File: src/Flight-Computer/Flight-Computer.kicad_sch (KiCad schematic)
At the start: 40 parts, among them J1 Jumper_NO, P1 282837-2, P2 647676-2, P8 3220-20-0200-00, U1 STM32H750VBTx, U2 LMS8117AMP-3.3_NOPB, Y1 ECS-240-18-33-JGN-TR

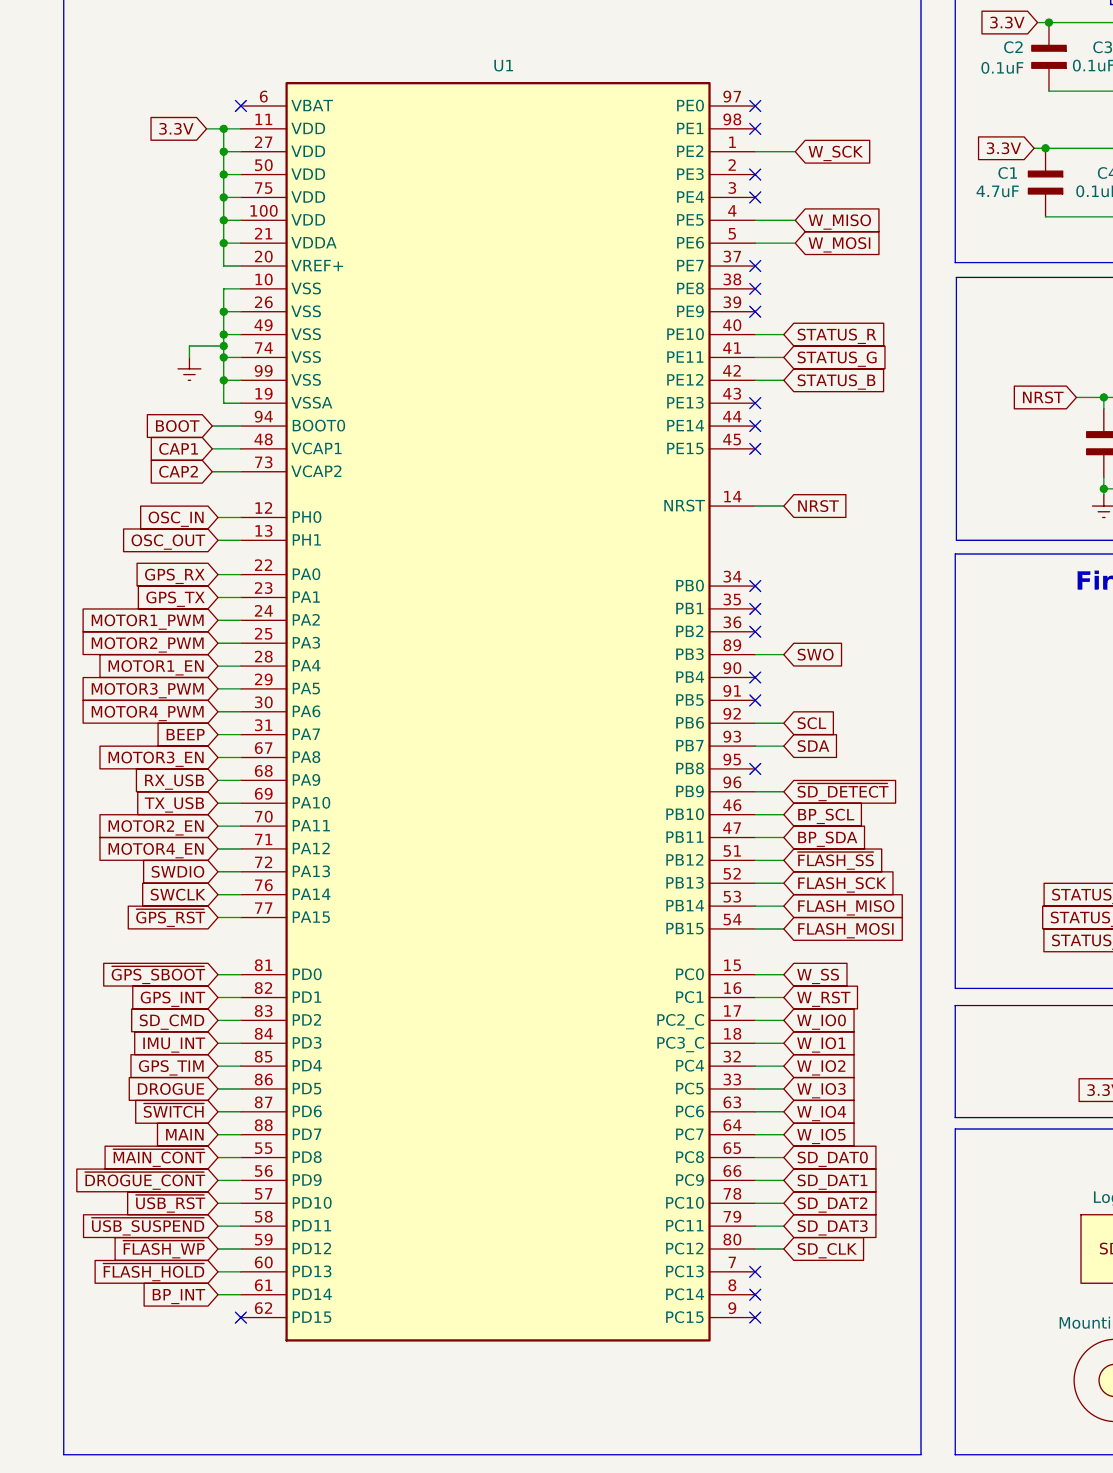
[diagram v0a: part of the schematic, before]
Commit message: routed main peripheral functionality excluding parachute deployment circuitry
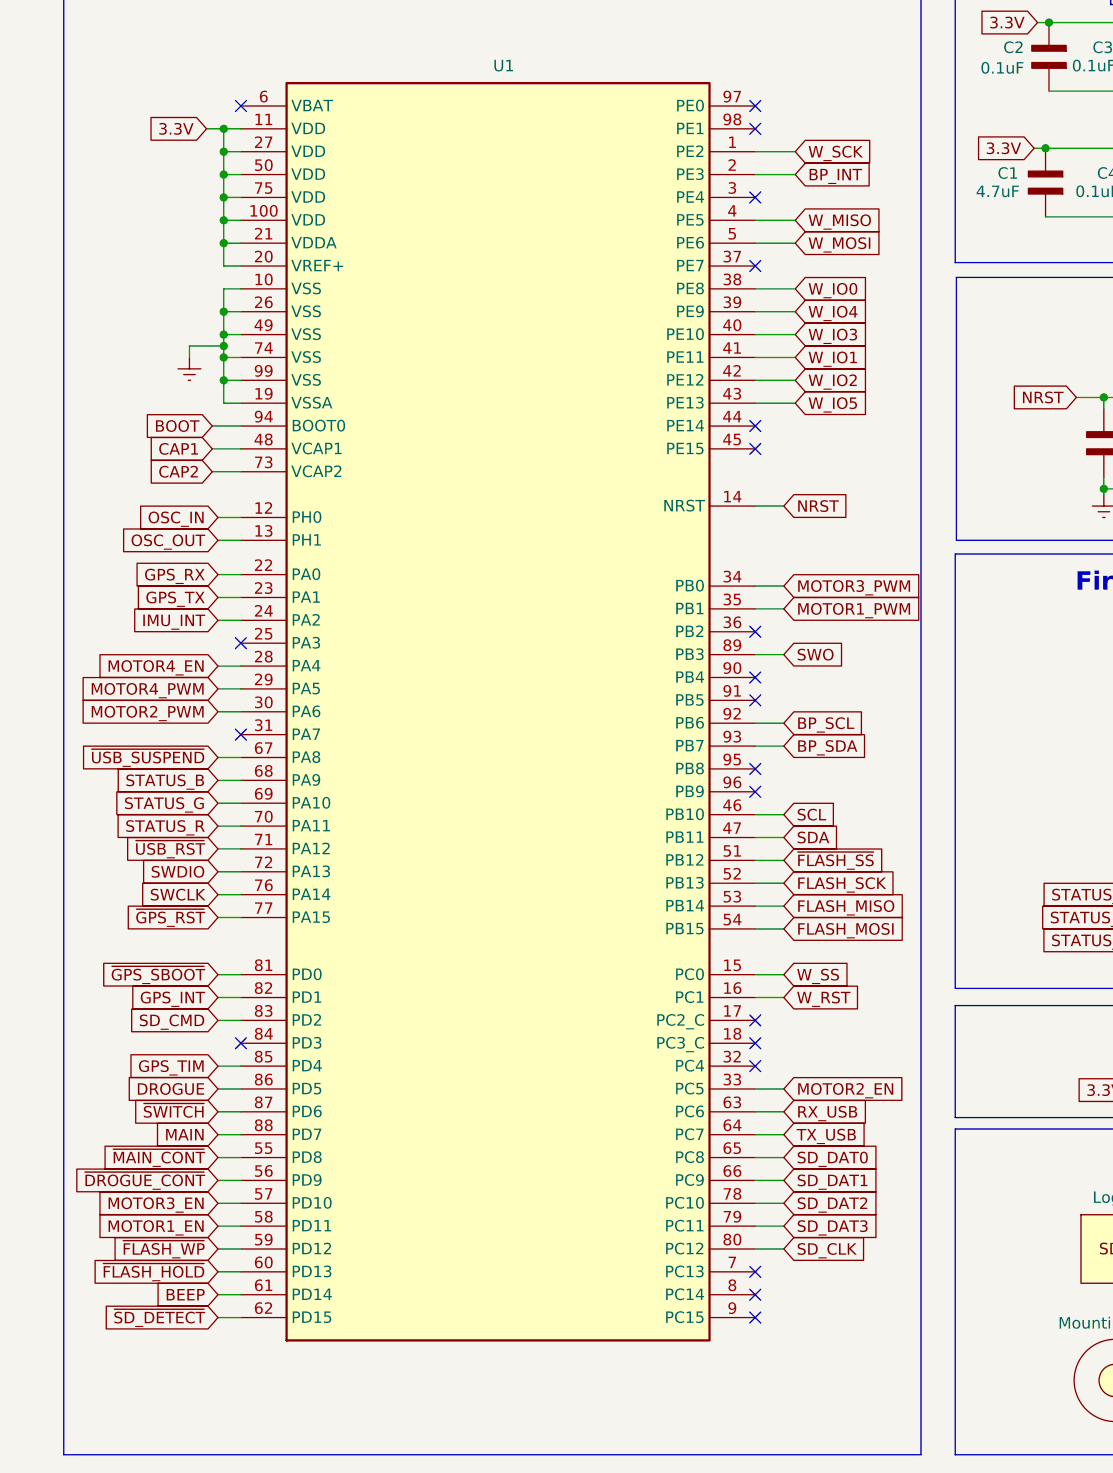
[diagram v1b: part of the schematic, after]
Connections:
- net BEEP: now also U1.61 (PD14); no longer U1.31 (PA7)
- net BP_INT: now also U1.2 (PE3); no longer U1.61 (PD14)
- net BP_SCL: now also U1.92 (PB6); no longer U1.46 (PB10)
- net BP_SDA: now also U1.93 (PB7); no longer U1.47 (PB11)
- net IMU_INT: now also U1.24 (PA2); no longer U1.84 (PD3)
- net MOTOR1_EN: now also U1.58 (PD11); no longer U1.28 (PA4)
- net MOTOR1_PWM: now also U1.35 (PB1); no longer U1.24 (PA2)
- net MOTOR2_EN: now also U1.33 (PC5); no longer U1.70 (PA11)
- net MOTOR2_PWM: now also U1.30 (PA6); no longer U1.25 (PA3)
- net MOTOR3_EN: now also U1.57 (PD10); no longer U1.67 (PA8)
- net MOTOR3_PWM: now also U1.34 (PB0); no longer U1.29 (PA5)
- net MOTOR4_EN: now also U1.28 (PA4); no longer U1.71 (PA12)
- net MOTOR4_PWM: now also U1.29 (PA5); no longer U1.30 (PA6)
- net RX_USB: now also U1.63 (PC6); no longer U1.68 (PA9)
- net SCL: now also U1.46 (PB10); no longer U1.92 (PB6)
- net SDA: now also U1.47 (PB11); no longer U1.93 (PB7)
- net STATUS_B: now also U1.68 (PA9); no longer U1.42 (PE12)
- net STATUS_G: now also U1.69 (PA10); no longer U1.41 (PE11)
- net STATUS_R: now also U1.70 (PA11); no longer U1.40 (PE10)
- net TX_USB: now also U1.64 (PC7); no longer U1.69 (PA10)
- net W_IO0: now also U1.38 (PE8); no longer U1.17 (PC2_C)
- net W_IO1: now also U1.41 (PE11); no longer U1.18 (PC3_C)
- net W_IO2: now also U1.42 (PE12); no longer U1.32 (PC4)
- net W_IO3: now also U1.40 (PE10); no longer U1.33 (PC5)
- net W_IO4: now also U1.39 (PE9); no longer U1.63 (PC6)
- net W_IO5: now also U1.43 (PE13); no longer U1.64 (PC7)
- net ~{SD_DETECT}: now also U1.62 (PD15); no longer U1.96 (PB9)
- net ~{USB_RST}: now also U1.71 (PA12); no longer U1.57 (PD10)
- net ~{USB_SUSPEND}: now also U1.67 (PA8); no longer U1.58 (PD11)

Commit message: finished routing
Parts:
- removed TP1: TP, Flight-Computer:TP, symbol Flight-Computer:TP
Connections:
- net DROGUE: now also U1.7 (PC13); no longer U1.86 (PD5)
- net GPS_INT: now also U1.25 (PA3); no longer U1.82 (PD1)
- net GPS_TIM: now also U1.32 (PC4); no longer U1.85 (PD4)
- net MAIN: now also U1.87 (PD6); no longer U1.88 (PD7)
- net W_IO1: now also U1.40 (PE10); no longer U1.41 (PE11)
- net W_IO3: now also U1.41 (PE11); no longer U1.40 (PE10)
- net ~{DROGUE_CONT}: now also U1.8 (PC14); no longer U1.56 (PD9)
- net ~{GPS_RST}: now also U1.31 (PA7); no longer U1.77 (PA15)
- net ~{GPS_SBOOT}: now also U1.9 (PC15); no longer U1.81 (PD0)
- net ~{MAIN_CONT}: now also U1.3 (PE4); no longer U1.55 (PD8)
- net ~{SWITCH}: now also U1.88 (PD7); no longer U1.87 (PD6)
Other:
- moved on the sheet: B1, C8

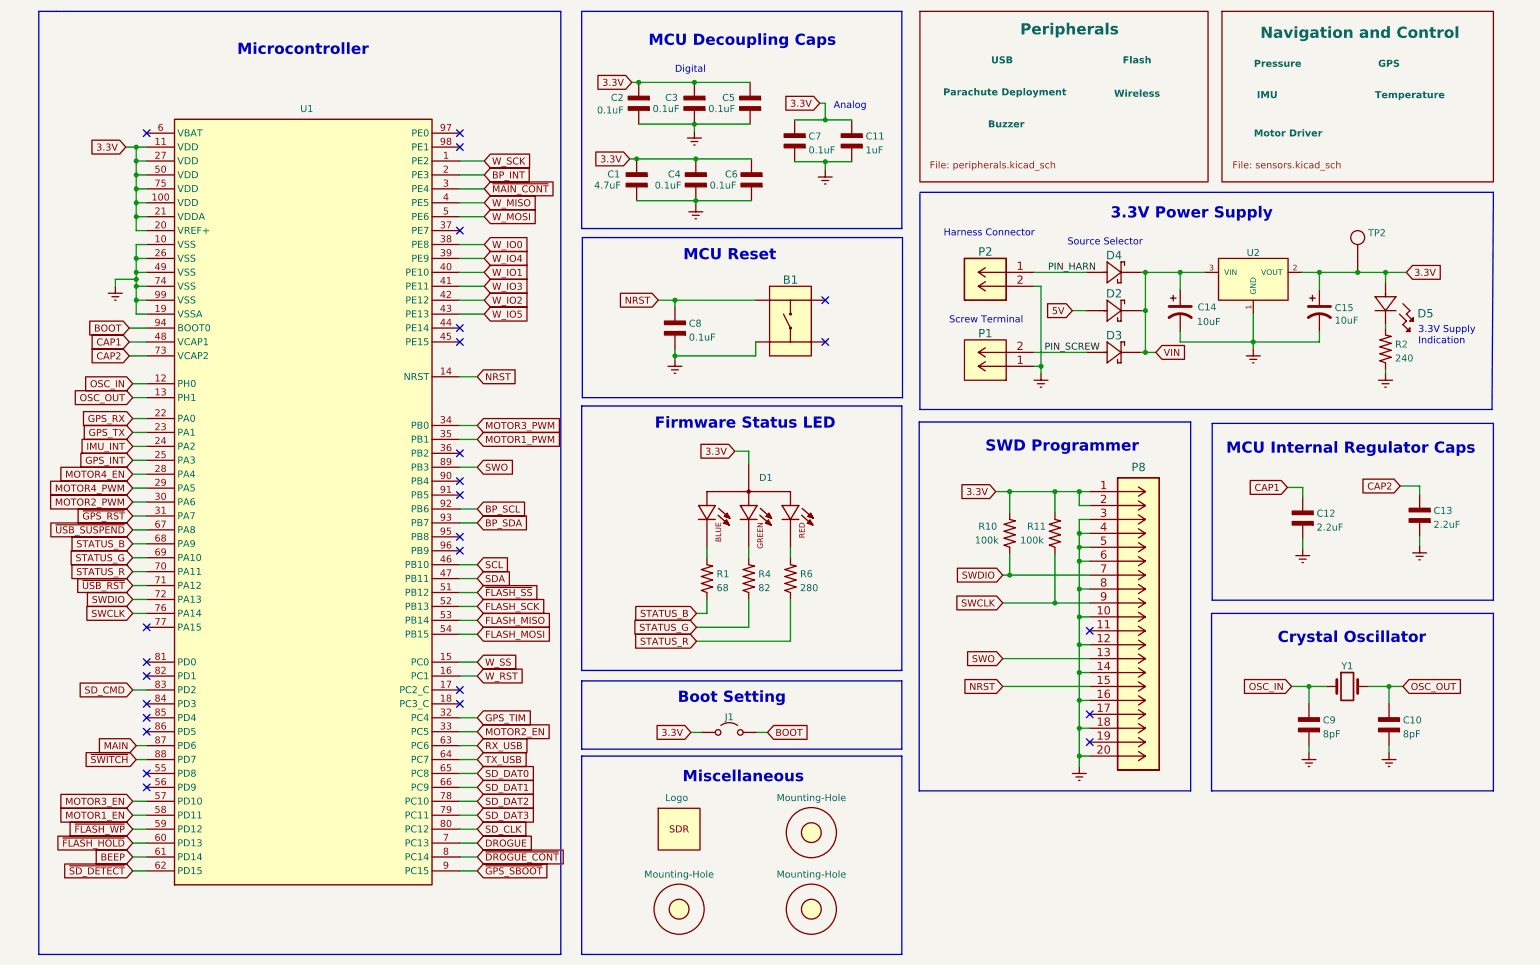
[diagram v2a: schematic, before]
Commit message: added usb detector to schemtaic
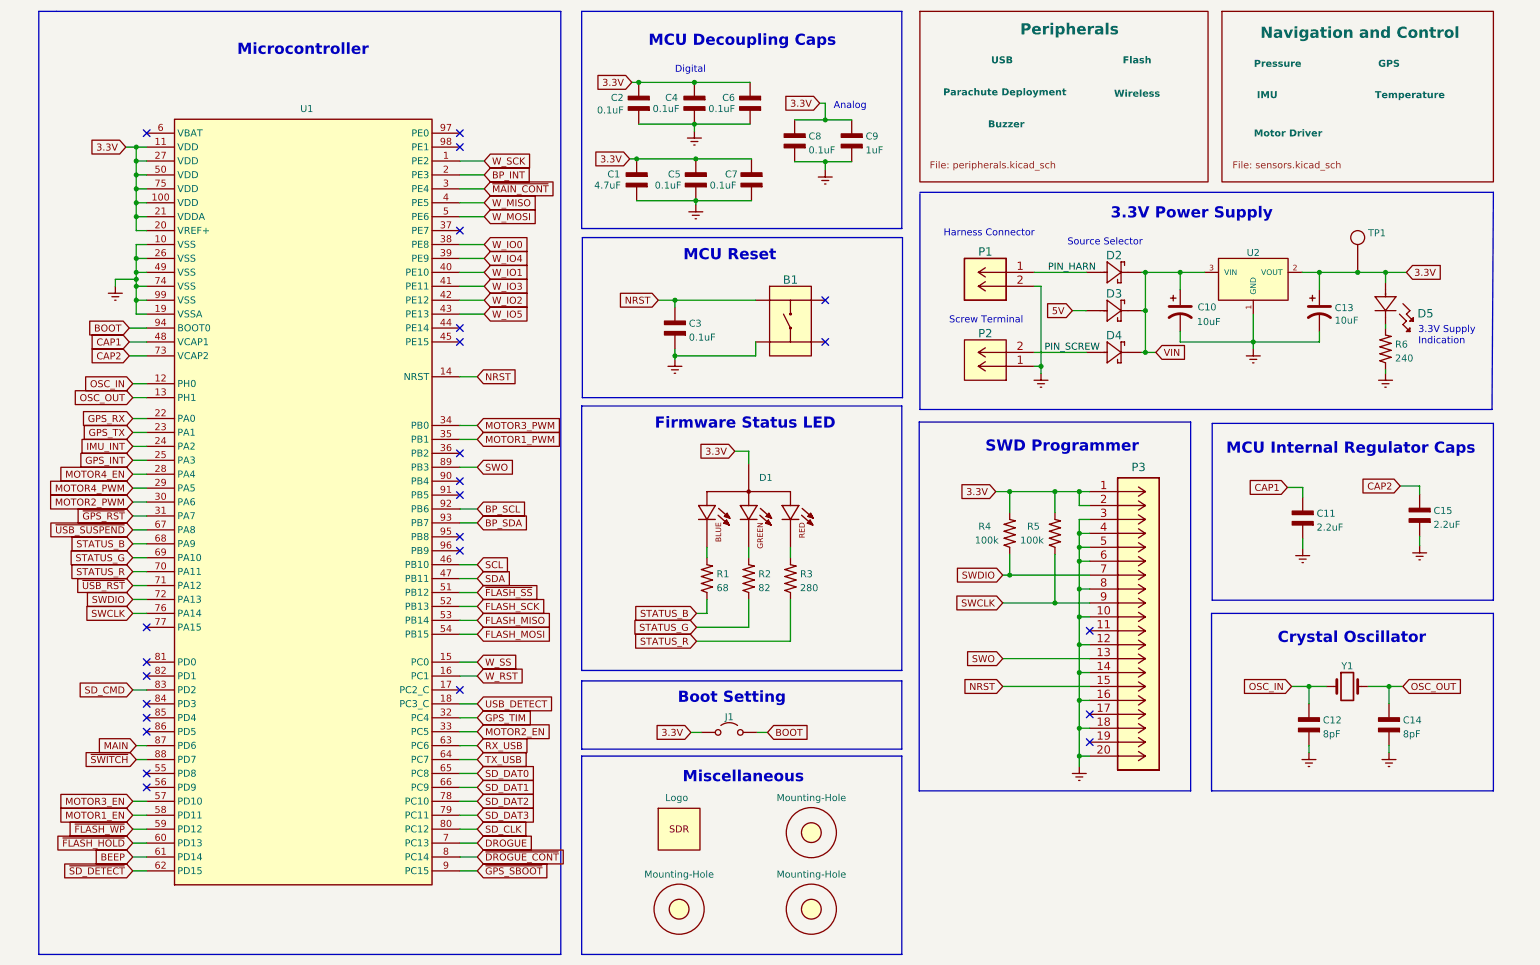
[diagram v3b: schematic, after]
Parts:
- renumbered C14 to C10, C12 to C11, C9 to C12, C15 to C13, C10 to C14, C13 to C15, C8 to C3, C3 to C4, C4 to C5, C5 to C6, C6 to C7, C7 to C8, C11 to C9, D4 to D2, D2 to D3, D3 to D4, H3 to H2, H4 to H3, P2 to P1, P1 to P2, P8 to P3, R4 to R2, R6 to R3, R10 to R4, R11 to R5, R2 to R6, TP2 to TP1
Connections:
- net USB_DETECT: now reaches U1.18 (PC3_C)
- no-connect marks 26 -> 25

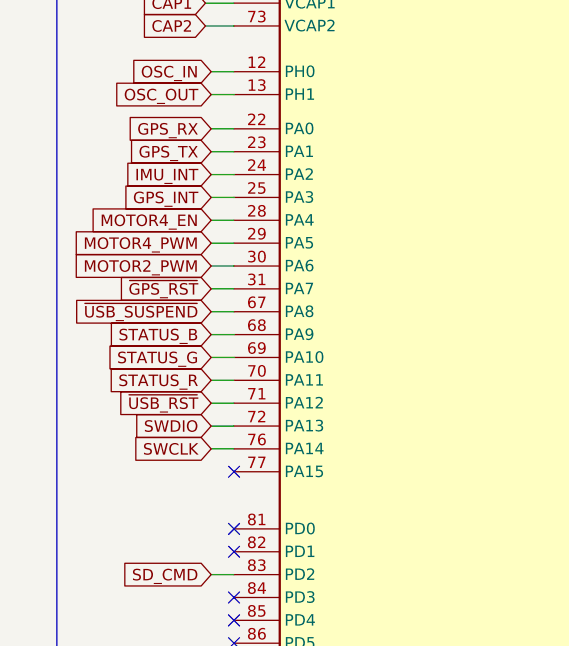
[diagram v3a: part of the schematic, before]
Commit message: implemented new imu in schematic
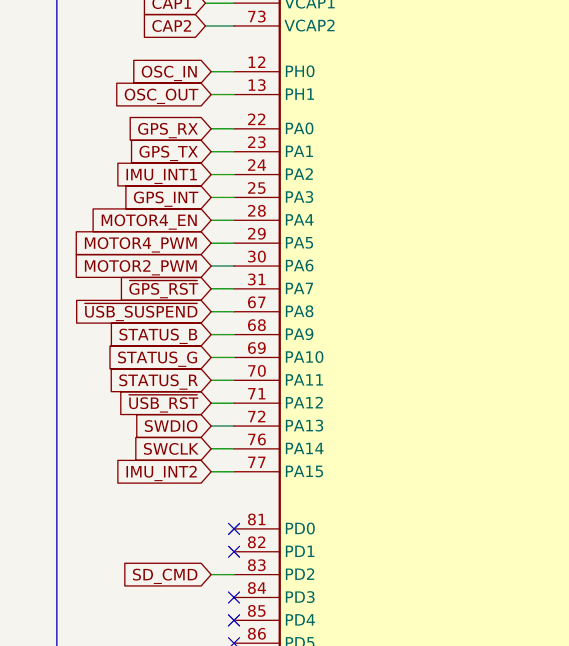
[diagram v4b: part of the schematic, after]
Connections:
- net IMU_INT2: now reaches U1.77 (PA15)
- net IMU_INT renamed IMU_INT1
- no-connect marks 25 -> 24
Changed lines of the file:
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@@
   (no_connect (at 36.195 160.655))
   (no_connect (at 93.345 79.375))
-  (no_connect (at 36.195 131.445))
   (no_connect (at 93.345 41.275))
   (no_connect (at 36.195 137.795))
@@
     (stroke (width 0) (type default) (color 0 0 0 0))
   )
+  (wire (pts (xy 33.655 131.445) (xy 36.195 131.445))
+    (stroke (width 0) (type default) (color 0 0 0 0))
+  )
   (wire (pts (xy 33.655 108.585) (xy 36.195 108.585))
     (stroke (width 0) (type default) (color 0 0 0 0))
@@
     )
   )
-  (global_label "IMU_INT" (shape input) (at 33.655 98.425 180) (fields_autoplaced)
-    (effects (font (size 1.27 1.27)) (justify right))
-    (property "Intersheet References" "${INTERSHEET_REFS}" (id 0) (at 24.0737 98.5044 0)
+  (global_label "IMU_INT1" (shape input) (at 33.655 98.425 180) (fields_autoplaced)
+    (effects (font (size 1.27 1.27)) (justify right))
+    (property "Intersheet References" "${INTERSHEET_REFS}" (id 0) (at 22.8641 98.3456 0)
       (effects (font (size 1.27 1.27)) (justify right) hide)
     )
@@
     (property "Intersheet References" "${INTERSHEET_REFS}" (id 0) (at 106.8271 163.1156 0)
       (effects (font (size 1.27 1.27)) (justify left) hide)
+    )
+  )
+  (global_label "IMU_INT2" (shape input) (at 33.655 131.445 180) (fields_autoplaced)
+    (effects (font (size 1.27 1.27)) (justify right))
+    (property "Intersheet References" "${INTERSHEET_REFS}" (id 0) (at 22.8641 131.3656 0)
+      (effects (font (size 1.27 1.27)) (justify right) hide)
     )
   )
@@
       (reference "#PWR016") (unit 1) (value "Earth") (footprint "")
     )
-    (path "/a7215684-cee9-4aba-87f1-e5962f77da19/1082dc28-77e5-4081-9653-ba3ccdcff140"
+    (path "/a7215684-cee9-4aba-87f1-e5962f77da19/9a733085-ccb6-4e9a-ae63-1f8c81139c23"
       (reference "#PWR017") (unit 1) (value "Earth") (footprint "")
     )
-    (path "/a7215684-cee9-4aba-87f1-e5962f77da19/3a528831-3703-47fa-b2f9-9d35d9a4482a"
+    (path "/a7215684-cee9-4aba-87f1-e5962f77da19/4f903274-7819-4ad4-9ef1-7cd0982c653d"
       (reference "#PWR018") (unit 1) (value "Earth") (footprint "")
     )
@@
       (reference "#PWR019") (unit 1) (value "Earth") (footprint "")
     )
-    (path "/a7215684-cee9-4aba-87f1-e5962f77da19/34f9584b-e14b-4f45-b1d8-6cf67f13081e"
-      (reference "#PWR020") (unit 1) (value "Earth") (footprint "")
-    )
-    (path "/a7215684-cee9-4aba-87f1-e5962f77da19/4bd954ef-7b24-4be2-9e47-dffb88431f61"
-      (reference "#PWR021") (unit 1) (value "Earth") (footprint "")
-    )
     (path "/a7215684-cee9-4aba-87f1-e5962f77da19/4b71cbdc-b374-4c43-a5ca-debee457df14"
       (reference "#PWR022") (unit 1) (value "Earth") (footprint "")
@@
       (reference "C16") (unit 1) (value "0.01uF") (footprint "Flight-Computer:CAP_0603")
     )
-    (path "/a7215684-cee9-4aba-87f1-e5962f77da19/ac484fe8-f18d-49d6-9d61-7cc144d8f31c"
+    (path "/a7215684-cee9-4aba-87f1-e5962f77da19/a0cd1c44-a6aa-4d8b-a2b3-df49039d37ee"
       (reference "C17") (unit 1) (value "0.1uF") (footprint "Flight-Computer:CAP_0603")
     )
-    (path "/a7215684-cee9-4aba-87f1-e5962f77da19/3008f6fe-df75-4af1-928e-60f268f36a31"
+    (path "/a7215684-cee9-4aba-87f1-e5962f77da19/6bf77307-b356-426a-b57a-ed29e912f1ea"
       (reference "C18") (unit 1) (value "0.1uF") (footprint "Flight-Computer:CAP_0603")
-    )
-    (path "/a7215684-cee9-4aba-87f1-e5962f77da19/470f33c1-72f7-44ac-be71-ff8826d723f3"
-      (reference "C19") (unit 1) (value "0.01uF") (footprint "Flight-Computer:CAP_0603")
     )
     (path "/a7215684-cee9-4aba-87f1-e5962f77da19/2bcd4158-516a-4eb6-9314-527fe16f509c"
@@
       (reference "R6") (unit 1) (value "240") (footprint "Flight-Computer:RES_0603")
     )
-    (path "/a7215684-cee9-4aba-87f1-e5962f77da19/830c687d-699c-4358-a76c-0906fd4cfd55"
-      (reference "R7") (unit 1) (value "10k") (footprint "Flight-Computer:RES_0603")
+    (path "/a7215684-cee9-4aba-87f1-e5962f77da19/a00a994e-144e-4867-8953-26047cca14b2"
+      (reference "R7") (unit 1) (value "10k") (footprint "")
     )
     (path "/a7215684-cee9-4aba-87f1-e5962f77da19/330c7051-badb-4c54-bd62-47706a91a7b3"
       (reference "R8") (unit 1) (value "10") (footprint "Flight-Computer:RES_0603")
     )
-    (path "/a7215684-cee9-4aba-87f1-e5962f77da19/bd93d9cd-28a3-48e0-865f-a80e4b2ada1a"
-      (reference "R9") (unit 1) (value "10k") (footprint "Flight-Computer:RES_0603")
+    (path "/a7215684-cee9-4aba-87f1-e5962f77da19/0f10209d-e80d-4264-9d1d-ea4f9620c93f"
+      (reference "R9") (unit 1) (value "10k") (footprint "")
     )
     (path "/a7215684-cee9-4aba-87f1-e5962f77da19/f6d57afb-9c72-4073-9e94-a358e99f15dc"
@@
       (reference "U2") (unit 1) (value "LMS8117AMP-3.3_NOPB") (footprint "Flight-Computer:LMS8117AMP-3.3NOPB")
     )
-    (path "/a7215684-cee9-4aba-87f1-e5962f77da19/efd68b6e-9e07-425c-97da-32faeda66c85"
-      (reference "U3") (unit 1) (value "MPU-9250") (footprint "Flight-Computer:MPU-9250")
+    (path "/a7215684-cee9-4aba-87f1-e5962f77da19/dd0328c6-3986-4941-b020-7d71cd718d1a"
+      (reference "U3") (unit 1) (value "BMI323") (footprint "Flight-Computer:BMI323")
     )
     (path "/a7215684-cee9-4aba-87f1-e5962f77da19/640e65b2-b4ce-424b-9b0b-d01f63d8cb07"
